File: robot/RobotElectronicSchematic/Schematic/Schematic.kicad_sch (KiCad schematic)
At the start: 21 parts, among them M1 Motor_DC, M2 Motor_DC, SW1 RotaryEncoder, SW2 RotaryEncoder, SW3 SW_Push, SW4 SW_Push, U1 ESP32-S3, U4 LSM6DS3

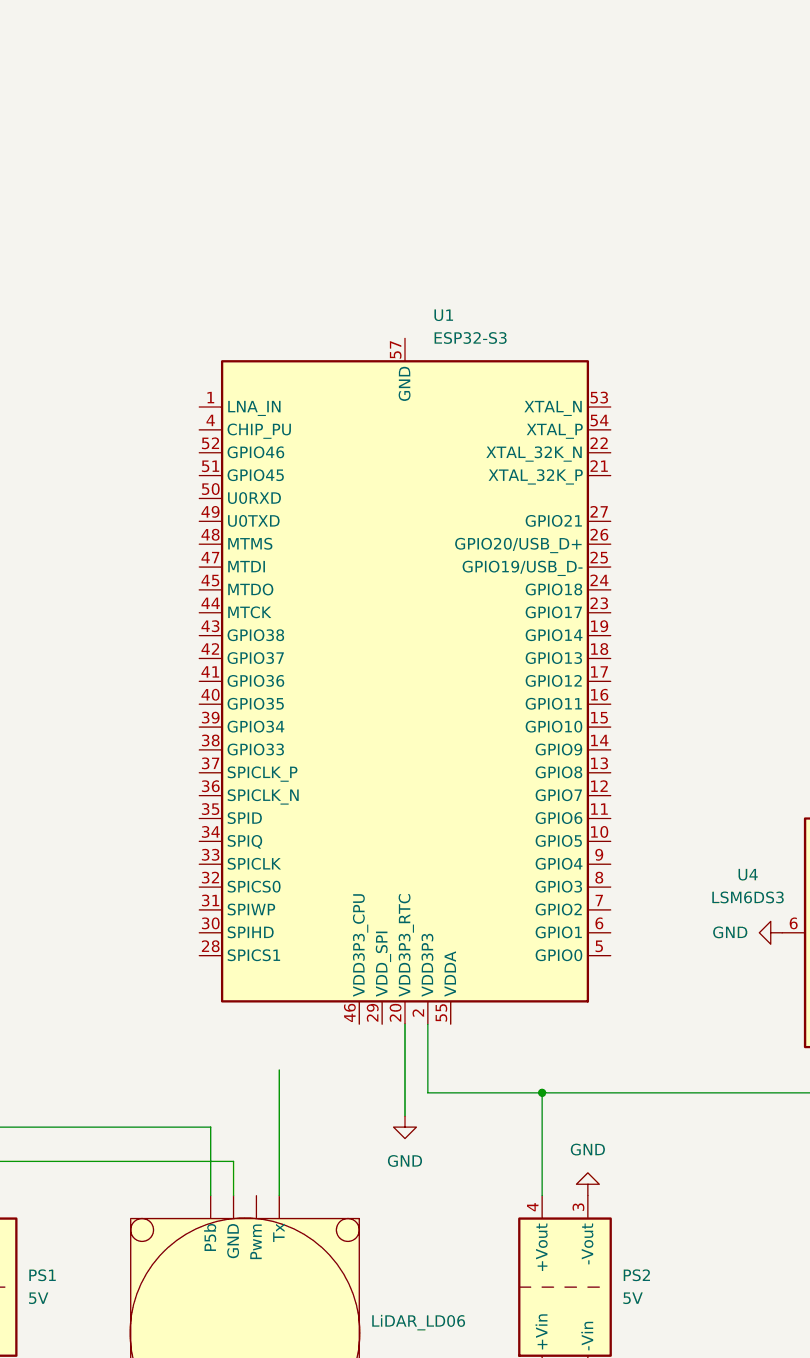
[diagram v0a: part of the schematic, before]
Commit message: restructurized some classes, added accelerometer data sending
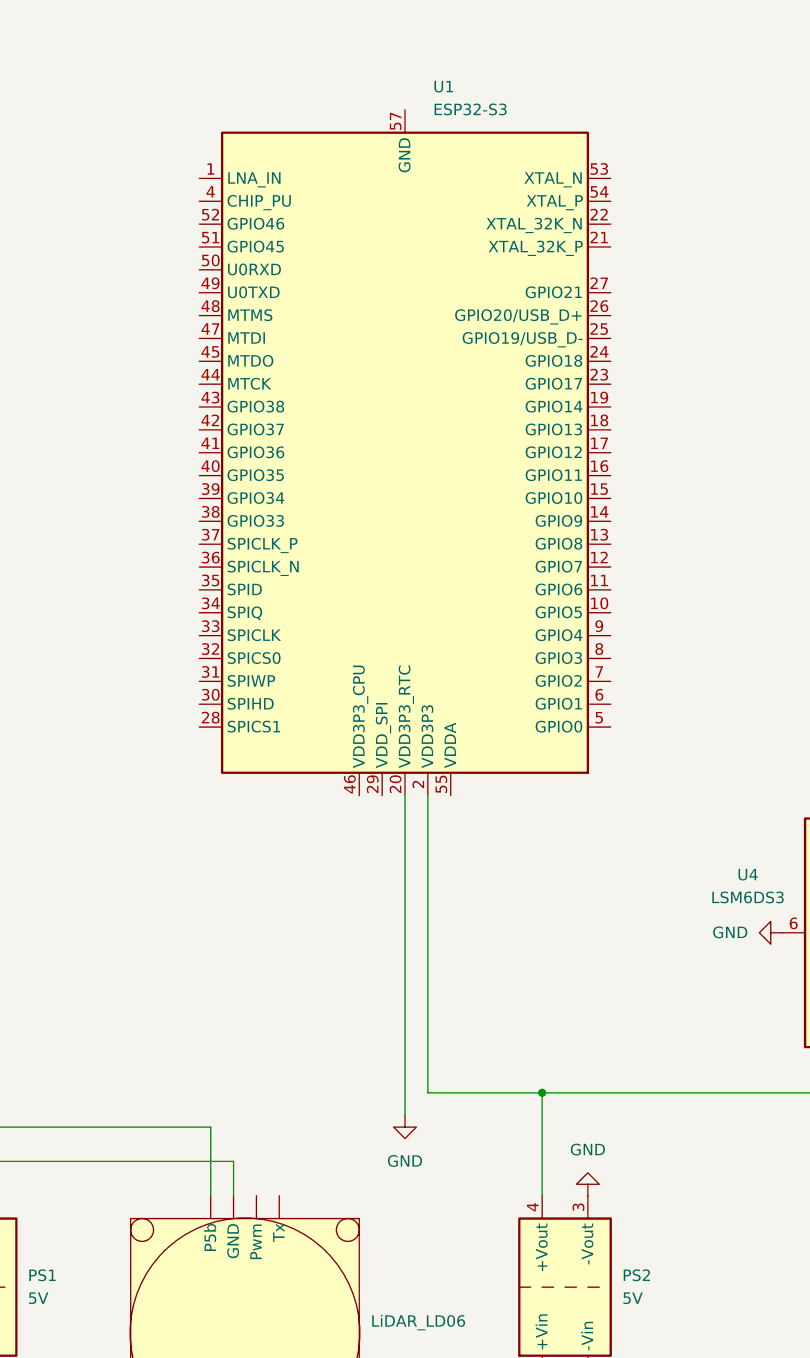
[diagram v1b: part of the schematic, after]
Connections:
- net at MosfetDriver2. (Vout+): now also MosfetDriver1. (Vout+), PS3.4 (+Vout)
- new net: MosfetDriver1. (Vout+), MosfetDriver2. (Vout+), PS3.3 (-Vout)
- now unconnected: MosfetDriver1. (Vout+), MosfetDriver1. (Vout+)
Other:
- moved on the sheet: U1
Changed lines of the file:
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@@
 	(wire
 		(pts
-			(xy 144.78 128.27) (xy 144.78 135.89)
+			(xy 144.78 102.87) (xy 144.78 135.89)
 		)
 		(stroke
@@
 	(wire
 		(pts
-			(xy 128.27 147.32) (xy 128.27 133.35)
-		)
-		(stroke
-			(width 0)
-			(type default)
-		)
-	)
-	(wire
-		(pts
 			(xy 157.48 167.64) (xy 157.48 177.8)
 		)
@@
 	(wire
 		(pts
-			(xy 142.24 128.27) (xy 142.24 138.43)
+			(xy 142.24 102.87) (xy 142.24 138.43)
 		)
 		(stroke
@@
 	(symbol
 		(lib_id "MCU_Espressif:ESP32-S3")
-		(at 142.24 90.17 180)
+		(at 142.24 64.77 180)
 		(unit 1)
 		(exclude_from_sim no)
@@
 		(fields_autoplaced yes)
 		(property "Reference" "U1"
-			(at 145.3581 49.53 0)
+			(at 145.3581 24.13 0)
 			(effects
 				(font
@@
 		)
 		(property "Value" "ESP32-S3"
-			(at 145.3581 52.07 0)
+			(at 145.3581 26.67 0)
 			(effects
 				(font
@@
 		)
 		(property "Footprint" "Package_DFN_QFN:QFN-56-1EP_7x7mm_P0.4mm_EP4x4mm"
-			(at 142.24 41.91 0)
+			(at 142.24 16.51 0)
 			(effects
 				(font
@@
 		)
 		(property "Datasheet" "https://www.espressif.com/sites/default/files/documentation/esp32-s3_datasheet_en.pdf"
-			(at 142.24 90.17 0)
+			(at 142.24 64.77 0)
 			(effects
 				(font
@@
 		)
 		(property "Description" "Microcontroller, Wi-Fi 802.11b/g/n, Bluetooth, 32bit"
-			(at 142.24 90.17 0)
-			(effects
-				(font
+			(at 142.24 64.77 0)
+			(effects
+				(font

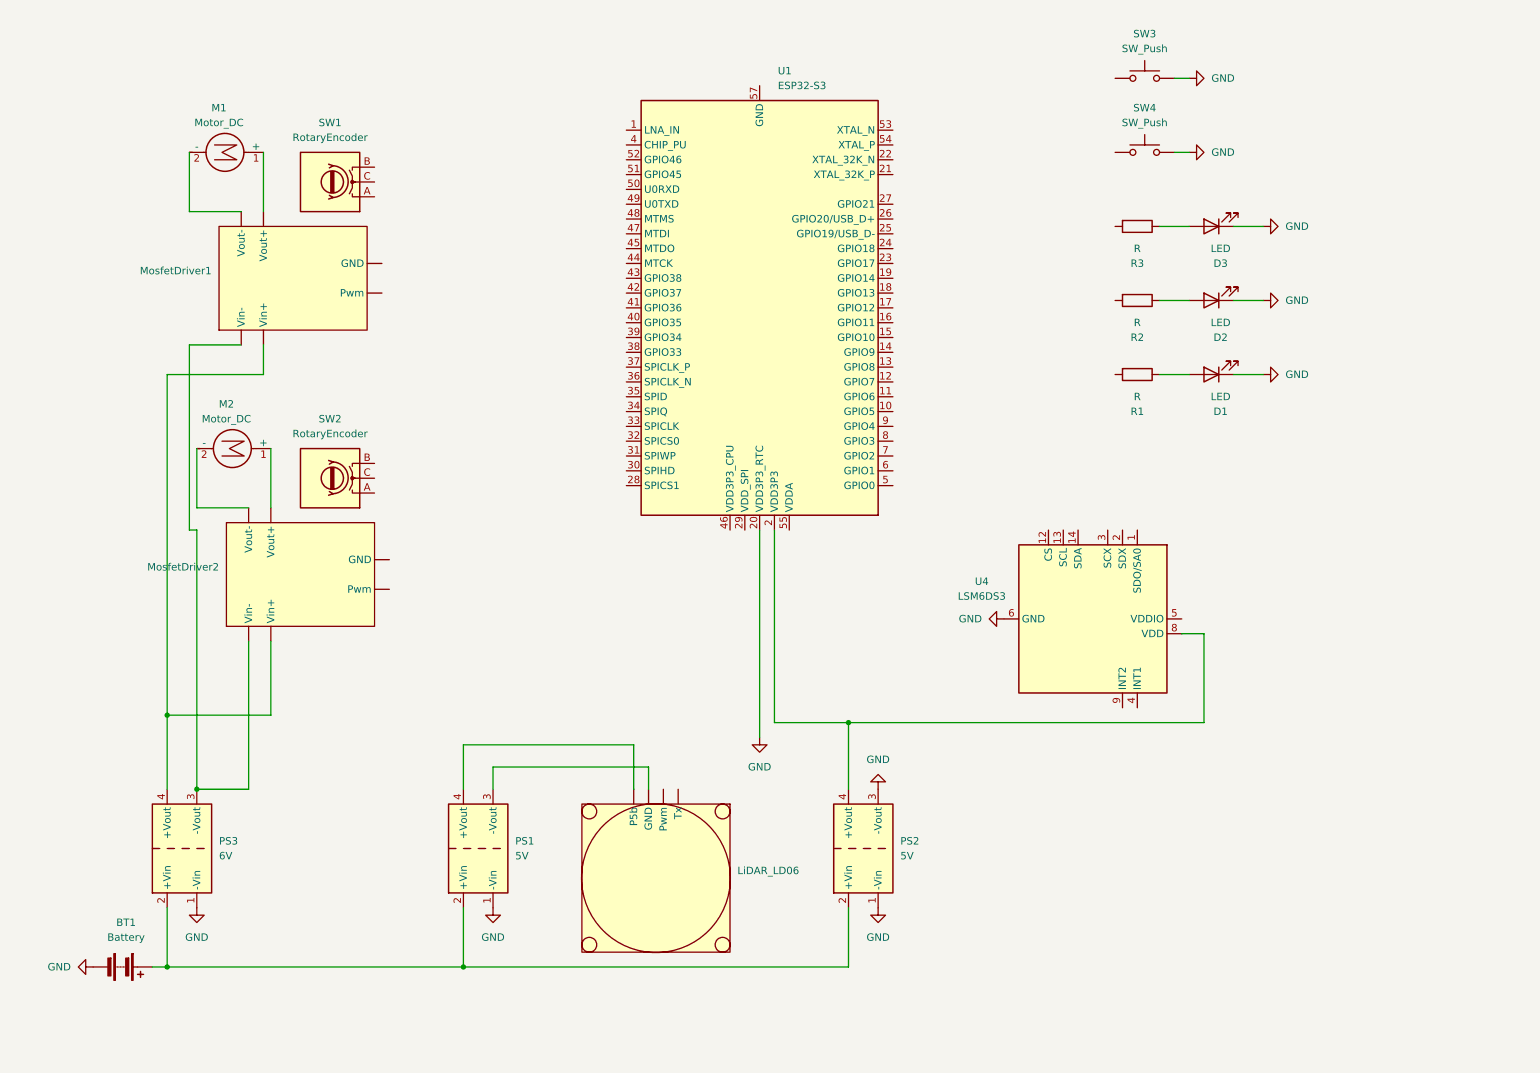
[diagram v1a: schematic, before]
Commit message: updated electronic chematic
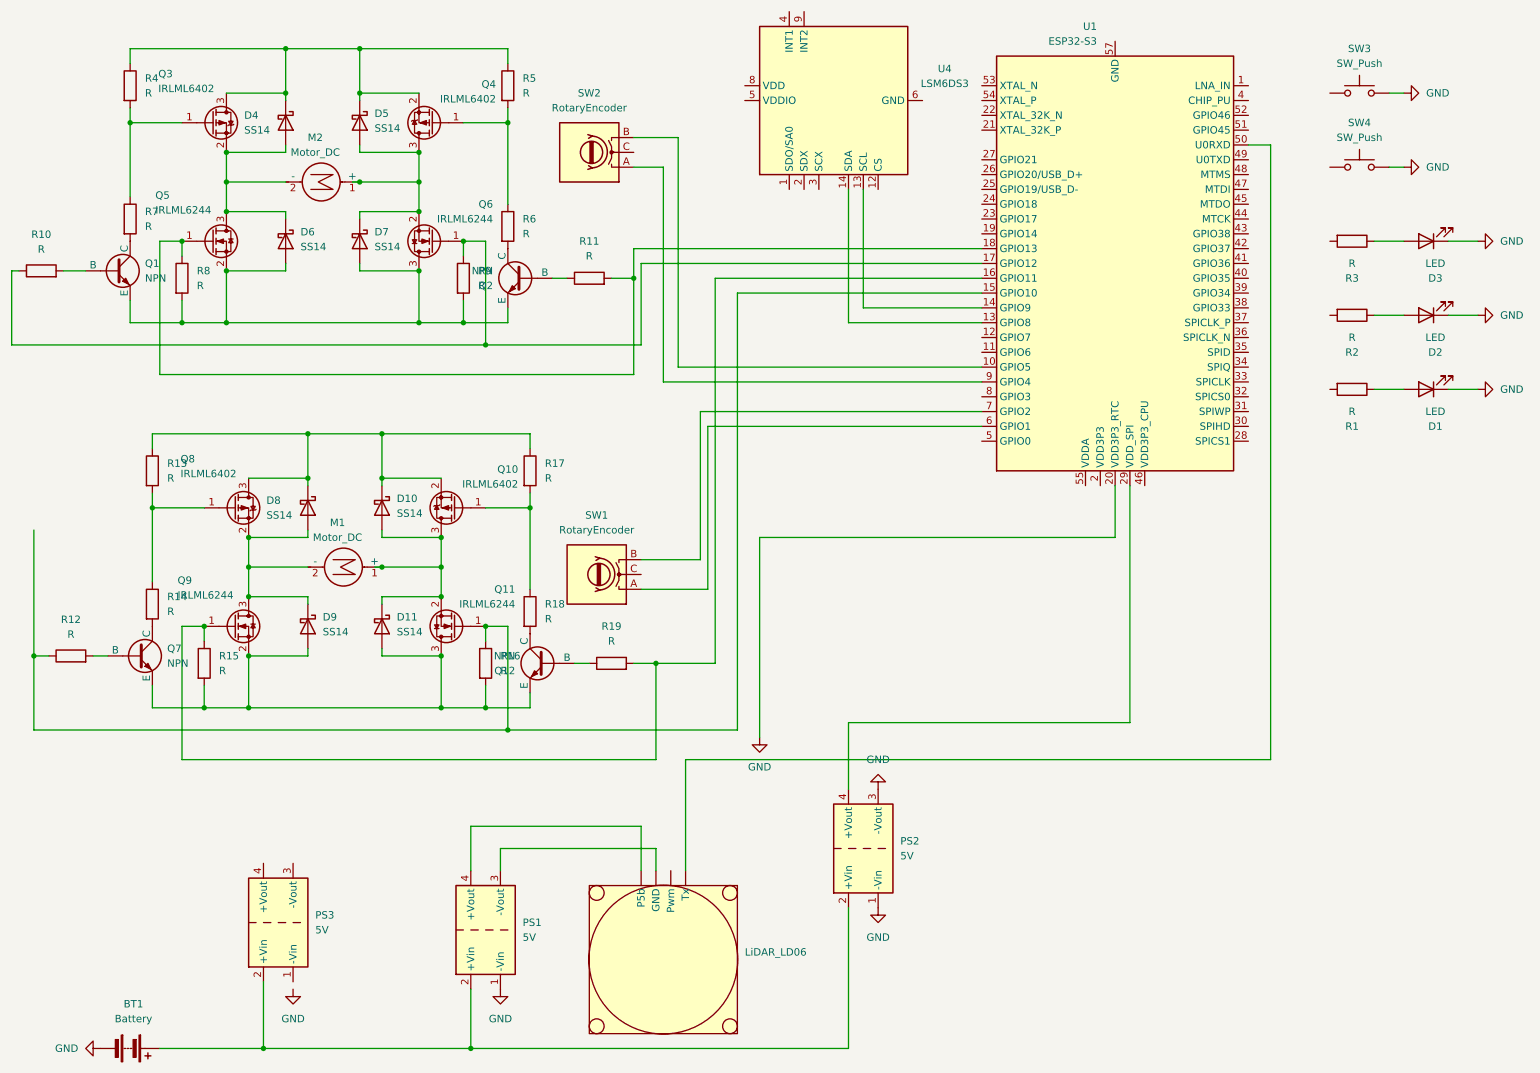
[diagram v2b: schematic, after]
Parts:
- removed M2: Motor_DC, symbol Motor:Motor_DC
- removed MosfetDriver1, MosfetDriver2: ~, symbol my_library:mosfet_driver
- added D10, D11, D4, D5, D6, D7, D8, D9: SS14, Diode_SMD:D_SMA, symbol Diode:SS14
- added M1: Motor_DC, symbol Motor:Motor_DC
- added Q1, Q12, Q2, Q7: NPN, symbol Simulation_SPICE:NPN
- added Q10, Q3, Q4, Q8: IRLML6402, Package_TO_SOT_SMD:SOT-23, symbol Transistor_FET:IRLML6402
- added Q11, Q5, Q6, Q9: IRLML6244, Package_TO_SOT_SMD:SOT-23, symbol Transistor_FET:IRLML6244
- added R10, R11, R12, R13, R14, R15, R16, R17, R18, R19, R4, R5, R6, R7, R8, R9: R, symbol Device:R
- PS3: value 6V -> 5V
- renumbered M1 to M2
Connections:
- net GND: no longer PS3.1 (-Vin), U4.6 (GND), U4.7 (GND)
- net at LiDAR_LD06. (P5b): now also U1.50 (U0RXD)
- net at U4.13 (SCL): now also U1.14 (GPIO9)
- net at U4.14 (SDA): now also U1.13 (GPIO8)
- net at U1.2 (VDD3P3), U1.3 (VDD3P3): no longer PS2.4 (+Vout), U4.8 (VDD)
- net at SW2.A: now also U1.9 (GPIO4)
- net at SW2.B: now also U1.10 (GPIO5)
- net at M2.1 (+): now also D5.2 (A), D7.1 (K), Q4.3 (D), Q6.2 (S)
- net at M2.2 (-): now also D4.2 (A), D6.1 (K), Q3.2 (S), Q5.3 (D)
- net at U1.15 (GPIO10): now also Q11.1 (G), R12.1, R16.1
- net at U1.16 (GPIO11): now also Q9.1 (G), R15.1, R19.2
- net at U1.17 (GPIO12): now also Q6.1 (G), R10.1, R9.1
- net at U1.18 (GPIO13): now also Q5.1 (G), R11.2, R8.1
- net at U1.29 (VDD_SPI): now also PS2.4 (+Vout)
- net at U1.6 (GPIO1): now also SW1.A
- net at U1.7 (GPIO2): now also SW1.B
- new net: D8.2 (A), D9.1 (K), M1.2 (-), Q8.2 (S), Q9.3 (D)
- new net: D11.2 (A), D9.2 (A), Q11.3 (D), Q12.3 (E), Q7.3 (E), Q9.2 (S), R15.2, R16.2
- new net: Q8.1 (G), R13.2, R14.1
- new net: D10.1 (K), D8.1 (K), Q10.2 (S), Q8.3 (D), R13.1, R17.1
- new net: Q7.2 (B), R12.2
- new net: Q2.2 (B), R11.1
- new net: D10.2 (A), D11.1 (K), M1.1 (+), Q10.3 (D), Q11.2 (S)
- new net: Q3.1 (G), R4.2, R7.1
- new net: D4.1 (K), D5.1 (K), Q3.3 (D), Q4.2 (S), R4.1, R5.1
- new net: Q7.1 (C), R14.2
- new net: Q1.1 (C), R7.2
- new net: Q1.2 (B), R10.2
- new net: D6.2 (A), D7.2 (A), Q1.3 (E), Q2.3 (E), Q5.2 (S), Q6.3 (D), R8.2, R9.2
- new net: Q4.1 (G), R5.2, R6.1
- new net: Q12.2 (B), R19.1
- new net: Q12.1 (C), R18.2
- new net: U4.6 (GND), U4.7 (GND)
- new net: Q2.1 (C), R6.2
- new net: Q10.1 (G), R17.2, R18.1
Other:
- moved on the sheet: BT1, D1, D2, D3, LiDAR_LD06, M2, PS1, R1, R2, R3, SW1, SW3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
